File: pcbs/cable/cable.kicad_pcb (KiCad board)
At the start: 2 copper layers, 16 x 28 mm, 1 part, among them J1 Conn_01x10_Pin

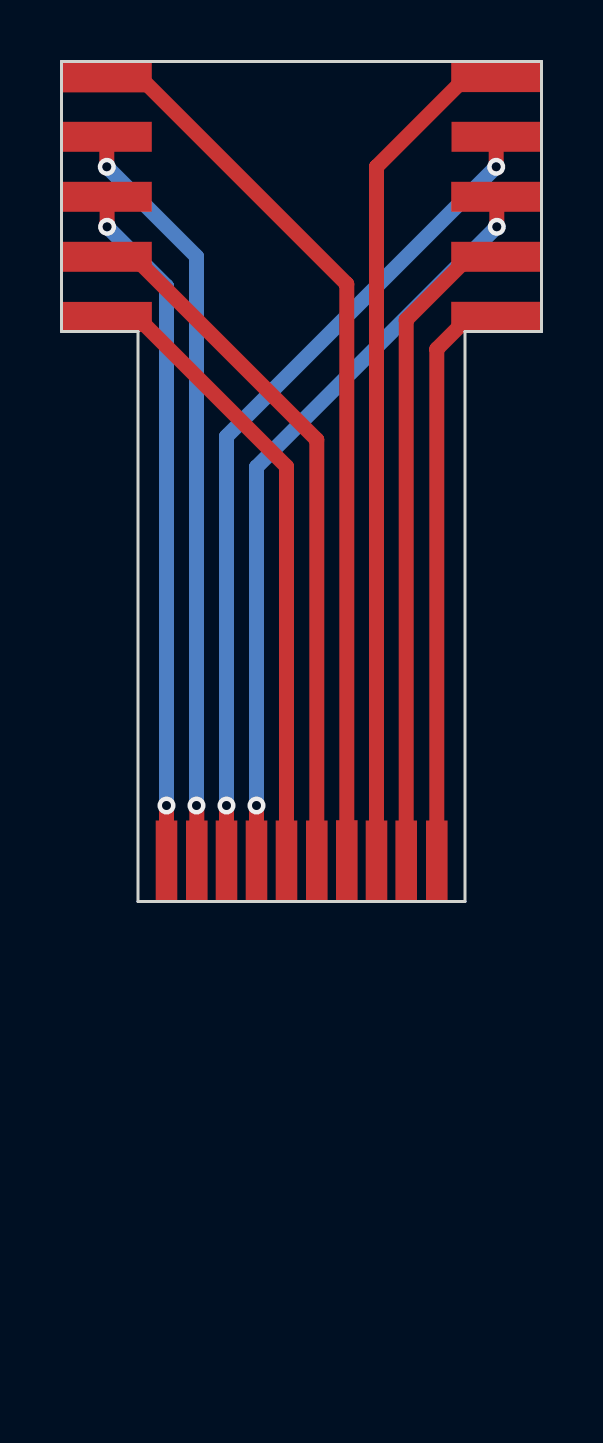
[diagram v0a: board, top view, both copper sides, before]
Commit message: lengthened display cable
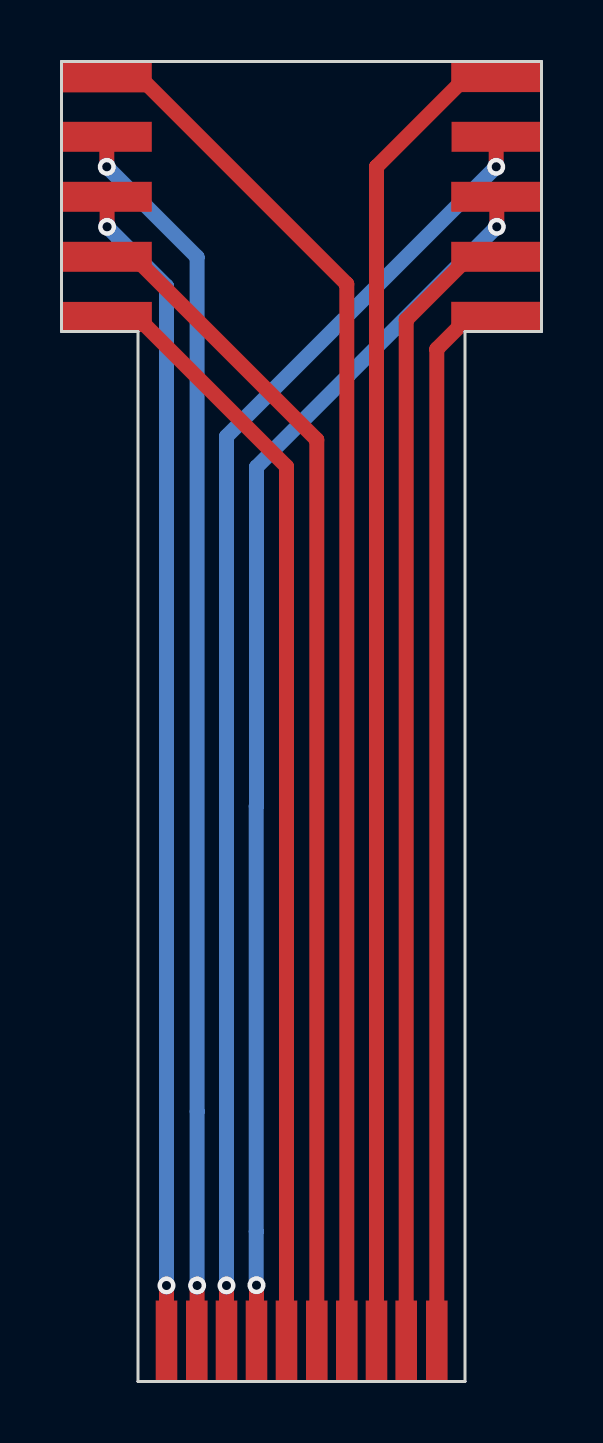
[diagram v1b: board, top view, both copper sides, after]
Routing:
- net unconnected-(J1-PadH3): track 27.8 -> 43.9 mm
- net unconnected-(J1-PadH2): track 25.4 -> 41.4 mm
- net unconnected-(J1-PadH4): track 25.5 -> 41.5 mm
- net unconnected-(J1-PadG2T): track 30.1 -> 46.1 mm
- net unconnected-(J1-PadG3T): track 19.5 -> 35.5 mm
- net unconnected-(J1-PadG3B): track 21.9 -> 37.9 mm
- net unconnected-(J1-PadG2B): track 28.4 -> 44.4 mm
- net unconnected-(J1-PadG1T): track 21.2 -> 37.2 mm
- net unconnected-(J1-PadH1): track 23.0 -> 39.0 mm
- net unconnected-(J1-PadG1B): track 23.6 -> 39.6 mm
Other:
- board size 16 x 28 mm -> 16 x 44 mm
